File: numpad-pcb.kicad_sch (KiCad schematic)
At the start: 20 parts, among them J1 AVR-ISP-6, SW1 SW_Push, U1 ATmega32U4-A, Y1 Crystal_GND24_Small

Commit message: Update PCB to show schematic changes
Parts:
- C1, C2, C3, C4, C5, C6, C7: footprint (none) -> Capacitor_SMD:C_0805_2012Metric_Pad1.18x1.45mm_HandSolder
- F1: footprint (none) -> Fuse:Fuse_1206_3216Metric_Pad1.42x1.75mm_HandSolder
- J1: footprint (none) -> random-keyboard-parts:Reset_Pretty-Mask
- R1, R2, R3, R4, R5, R6: footprint (none) -> Resistor_SMD:R_0805_2012Metric_Pad1.20x1.40mm_HandSolder
- SW1: footprint (none) -> Alps_Only:ALPS-1U
- USB1: footprint (none) -> Type-C:HRO-TYPE-C-31-M-12-HandSoldering
- Y1: footprint (none) -> Crystal:Crystal_SMD_3225-4Pin_3.2x2.5mm_HandSoldering
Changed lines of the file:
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@@
 			)
 		)
-		(property "Footprint" ""
+		(property "Footprint" "Resistor_SMD:R_0805_2012Metric_Pad1.20x1.40mm_HandSolder"
 			(at 161.29 102.87 0)
 			(effects
@@
 			)
 		)
-		(property "Footprint" ""
+		(property "Footprint" "Alps_Only:ALPS-1U"
 			(at 106.68 29.21 0)
 			(effects
@@
 			)
 		)
-		(property "Footprint" ""
+		(property "Footprint" "Capacitor_SMD:C_0805_2012Metric_Pad1.18x1.45mm_HandSolder"
 			(at 71.12 88.9 0)
 			(effects
@@
 			)
 		)
-		(property "Footprint" ""
+		(property "Footprint" "Crystal:Crystal_SMD_3225-4Pin_3.2x2.5mm_HandSoldering"
 			(at 113.03 57.15 0)
 			(effects
@@
 			)
 		)
-		(property "Footprint" ""
+		(property "Footprint" "Capacitor_SMD:C_0805_2012Metric_Pad1.18x1.45mm_HandSolder"
 			(at 102.87 60.96 0)
 			(effects
@@
 			)
 		)
-		(property "Footprint" ""
+		(property "Footprint" "Capacitor_SMD:C_0805_2012Metric_Pad1.18x1.45mm_HandSolder"
 			(at 102.87 49.53 0)
 			(effects
@@
 			)
 		)
-		(property "Footprint" ""
+		(property "Footprint" "Resistor_SMD:R_0805_2012Metric_Pad1.20x1.40mm_HandSolder"
 			(at 113.03 29.21 0)
 			(effects
@@
 			)
 		)
-		(property "Footprint" ""
+		(property "Footprint" "Resistor_SMD:R_0805_2012Metric_Pad1.20x1.40mm_HandSolder"
 			(at 100.33 77.47 0)
 			(effects
@@
 			)
 		)
-		(property "Footprint" ""
+		(property "Footprint" "random-keyboard-parts:Reset_Pretty-Mask"
 			(at 170.18 33.02 90)
 			(effects
@@
 			)
 		)
-		(property "Footprint" ""
+		(property "Footprint" "Capacitor_SMD:C_0805_2012Metric_Pad1.18x1.45mm_HandSolder"
 			(at 81.28 88.9 0)
 			(effects
@@
 			)
 		)
-		(property "Footprint" ""
+		(property "Footprint" "Resistor_SMD:R_0805_2012Metric_Pad1.20x1.40mm_HandSolder"
 			(at 106.68 74.93 0)
 			(effects
@@
 			)
 		)
-		(property "Footprint" ""
+		(property "Footprint" "Resistor_SMD:R_0805_2012Metric_Pad1.20x1.40mm_HandSolder"
 			(at 73.66 133.35 0)
 			(effects
@@
 			)
 		)
-		(property "Footprint" ""
+		(property "Footprint" "Fuse:Fuse_1206_3216Metric_Pad1.42x1.75mm_HandSolder"
 			(at 83.82 109.22 0)
 			(effects
@@
 			)
 		)
-		(property "Footprint" ""
+		(property "Footprint" "Capacitor_SMD:C_0805_2012Metric_Pad1.18x1.45mm_HandSolder"
 			(at 62.23 88.9 0)
 			(effects
@@
 			)
 		)
-		(property "Footprint" ""
+		(property "Footprint" "Type-C:HRO-TYPE-C-31-M-12-HandSoldering"
 			(at 59.69 121.92 0)
 			(effects
@@
 			)
 		)
-		(property "Footprint" ""
+		(property "Footprint" "Resistor_SMD:R_0805_2012Metric_Pad1.20x1.40mm_HandSolder"
 			(at 77.47 133.35 0)
 			(effects
@@
 			)
 		)
-		(property "Footprint" ""
+		(property "Footprint" "Capacitor_SMD:C_0805_2012Metric_Pad1.18x1.45mm_HandSolder"
 			(at 111.76 90.17 0)
 			(effects
@@
 			)
 		)
-		(property "Footprint" ""
+		(property "Footprint" "Capacitor_SMD:C_0805_2012Metric_Pad1.18x1.45mm_HandSolder"
 			(at 91.44 88.9 0)
 			(effects

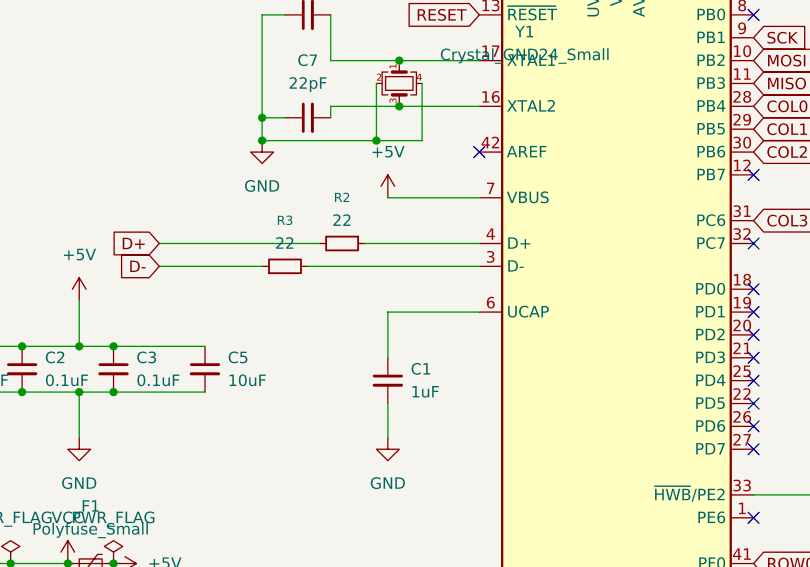
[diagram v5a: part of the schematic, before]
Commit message: Repair edge and bottom traces
Fixed the differential pair to have closer trace lengths (+/- 0.5 mm
reduced to 0.03 mm) for higher accuracy and error prevention. Also
created GND pour for crystal to reduce noise.
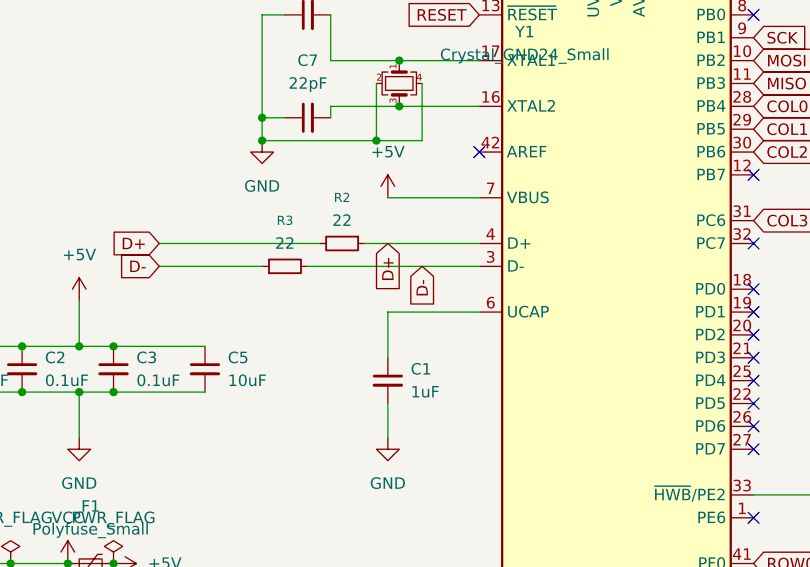
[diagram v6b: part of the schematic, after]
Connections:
- net D+: now also R2.1, U1.4 (D+)
- net D-: now also R3.2, U1.3 (D-)
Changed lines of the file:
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@@
+		)
+	)
+	(global_label "D-"
+		(shape input)
+		(at 115.57 77.47 270)
+		(fields_autoplaced yes)
+		(effects
+			(font
+				(size 1.27 1.27)
+			)
+			(justify right)
+		)
+		(property "Intersheetrefs" "${INTERSHEET_REFS}"
+			(at 115.57 83.2976 90)
+			(effects
+				(font
+					(size 1.27 1.27)
+				)
+				(justify right)
+				(hide yes)
+			)
+		)
+	)
+	(global_label "D+"
+		(shape input)
+		(at 111.76 74.93 270)
+		(fields_autoplaced yes)
+		(effects
+			(font
+				(size 1.27 1.27)
+			)
+			(justify right)
+		)
+		(property "Intersheetrefs" "${INTERSHEET_REFS}"
+			(at 111.76 80.7576 90)
+			(effects
+				(font
+					(size 1.27 1.27)
+				)
+				(justify right)
+				(hide yes)
+			)
 		)
 	)
